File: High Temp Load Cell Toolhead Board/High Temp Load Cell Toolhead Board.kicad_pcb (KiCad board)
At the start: 4 copper layers, 60 x 60 mm, 118 parts, among them J1 Conn_01x03, J11 Conn_01x03, J12 Conn_01x03, J13 PinHeader_2x4_P2.54mm, J2 Conn_02x08, J6 Conn_01x04, J7 Conn_01x02, J8 Conn_01x04, J9 Conn_01x02, P1 USB_C_Plug_USB2.0, Q1 DMG3404L, Q2 DMG3404L, SW1 SW_SPST, U1 MAX31865xTP, U2 STM32F103CBU6TR, U3 SN74LVC2G17DSFR, U4 SN74AHC1G32QDBVRQ1, U5 ADS1220, X1 ECS-2520MVLC-080-BP-TR

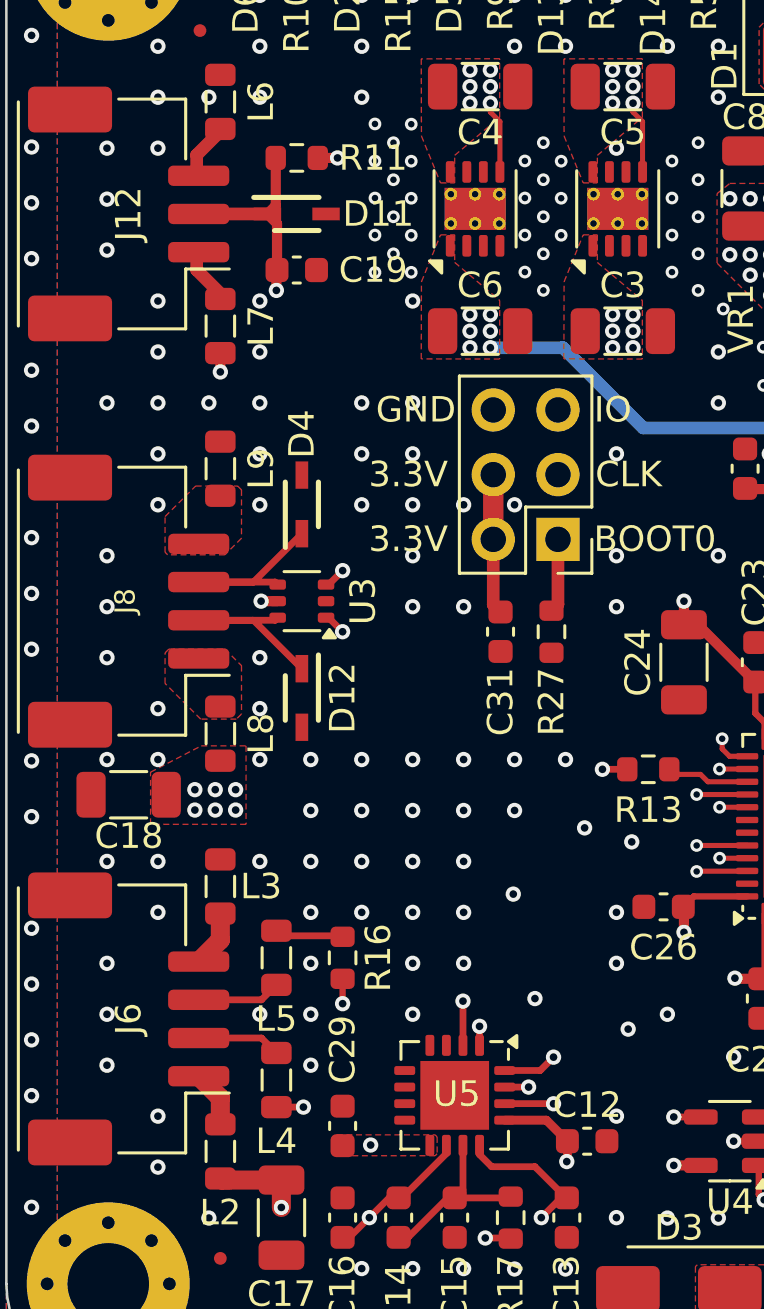
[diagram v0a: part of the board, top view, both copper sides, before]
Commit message: Add Net Class Directives
This change adds Net Class Directives for 3 types of specialized nets:
* ADC Signal - a net that may potentially be sensed by an ADC and should be treated as 50 Ohm impedance
* Digital Signal - a net that will have an oscillating digital signal on it but does not carry any power. This should also be treated as 50 Ohm impedance.
* Digital Pair - a differential digital pair. This is only used for the USB data pair which is 90 Ohm impedance.
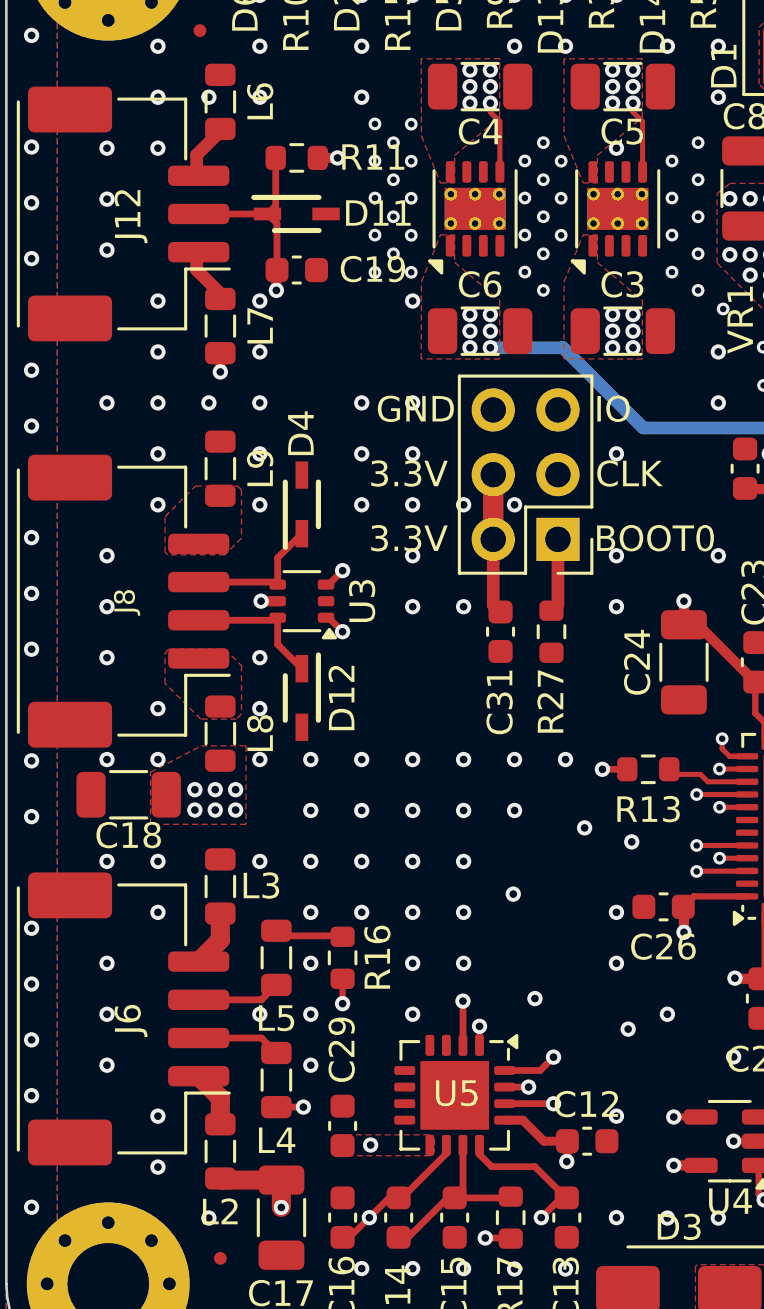
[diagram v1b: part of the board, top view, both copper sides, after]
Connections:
- net /INPUT_24V+ renamed /+24V_INPUT
- net /INPUT_FANV+ renamed /+FANV_INPUT
- net /SW_HEATSINK_4 renamed /SW_HEATSINK
- net SPI_2_SCLK renamed LED_MCU_CLK
- net SPI_2_SDO renamed LED_MCU_SDO
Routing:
- net /LED_SDI: track 7.98 -> 5.53 mm
- net /LED_CLK: track 7.98 -> 5.53 mm

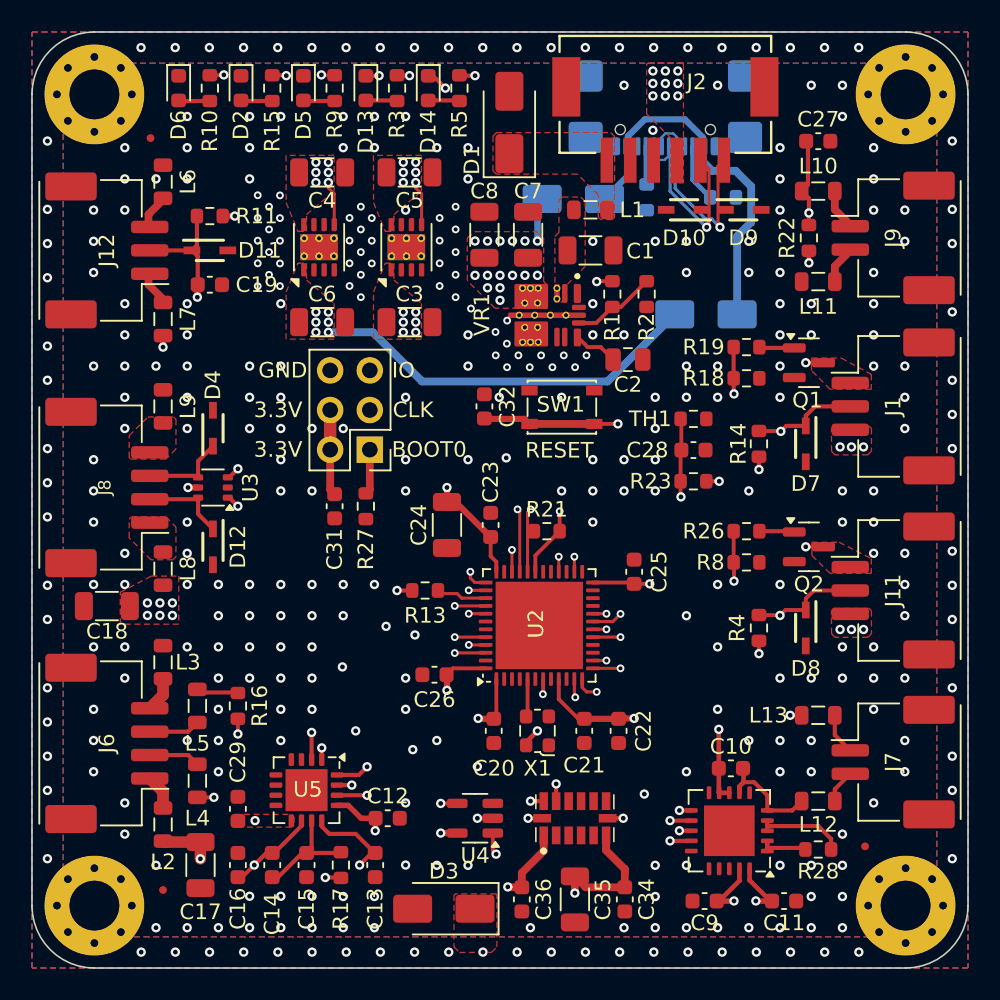
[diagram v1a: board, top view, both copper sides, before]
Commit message: More Targeted GND Paths
* Fix the TLVM23615RDNR footprint so its pads are plated
* Add GND vias in locations where via walls exist on layer 1
* Add GND vias or where a signal transitions across the core material between layer 2 and 3
* Add some GND vias near power decoupling capacitors
* Move the ADS1220 ADC signal lines down to layer 32 so they have 100% ground coverage across their length. They were passing under 5V caps and resistors.
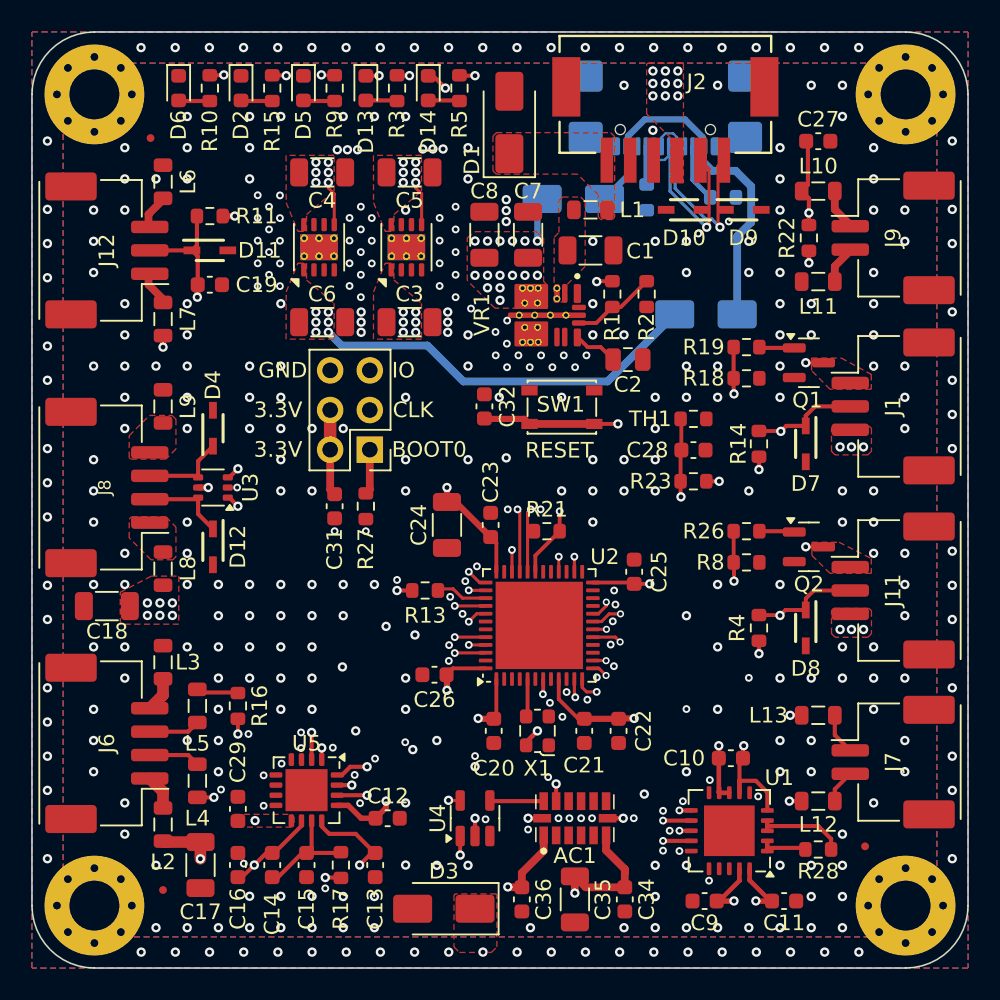
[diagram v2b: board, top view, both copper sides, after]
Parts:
- moved C10 0.65 mm to (44.8, 46.5)
- turned U4 to 90 degrees
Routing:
- net Net-(U1-FORCE+): track 7.77 -> 12.7 mm, vias 0 -> 2
- net Net-(AC1-SDA/SDI/SDIO): track 7.73 -> 3.47 mm, vias 2 -> 0
- net /FAN0_MOSFET_GND: track 46.3 -> 49.3 mm
- net /FAN1_MOSFET_GND: track 56.1 -> 59.0 mm
- net ADXL345_CS: track 21.8 -> 23.9 mm
- net SPI_1_SCLK: track 44.3 -> 43.1 mm
- net MAX31865_CS: track 17.7 -> 16.5 mm
- net USB_PULL_UP: track 47.4 -> 46.7 mm
- net Net-(U1-FORCE-): track 10.4 -> 9.79 mm
- net GND: vias 273 -> 340

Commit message: USB Routing Improvement & Trach Width Change
* Fix net class assignment of USB lines so they autoroute with the correct rules.
* Moved the LED CLK line routing so it doesn't cross the USB lines
* Added a zone of ground fill on layer 3 to cover the USB traces on the back of the board
* Changes the standard track with to 15mil / 0.381mm. This is what OSH Park say is 50 Ohm in their process.

Fixup

Fixup
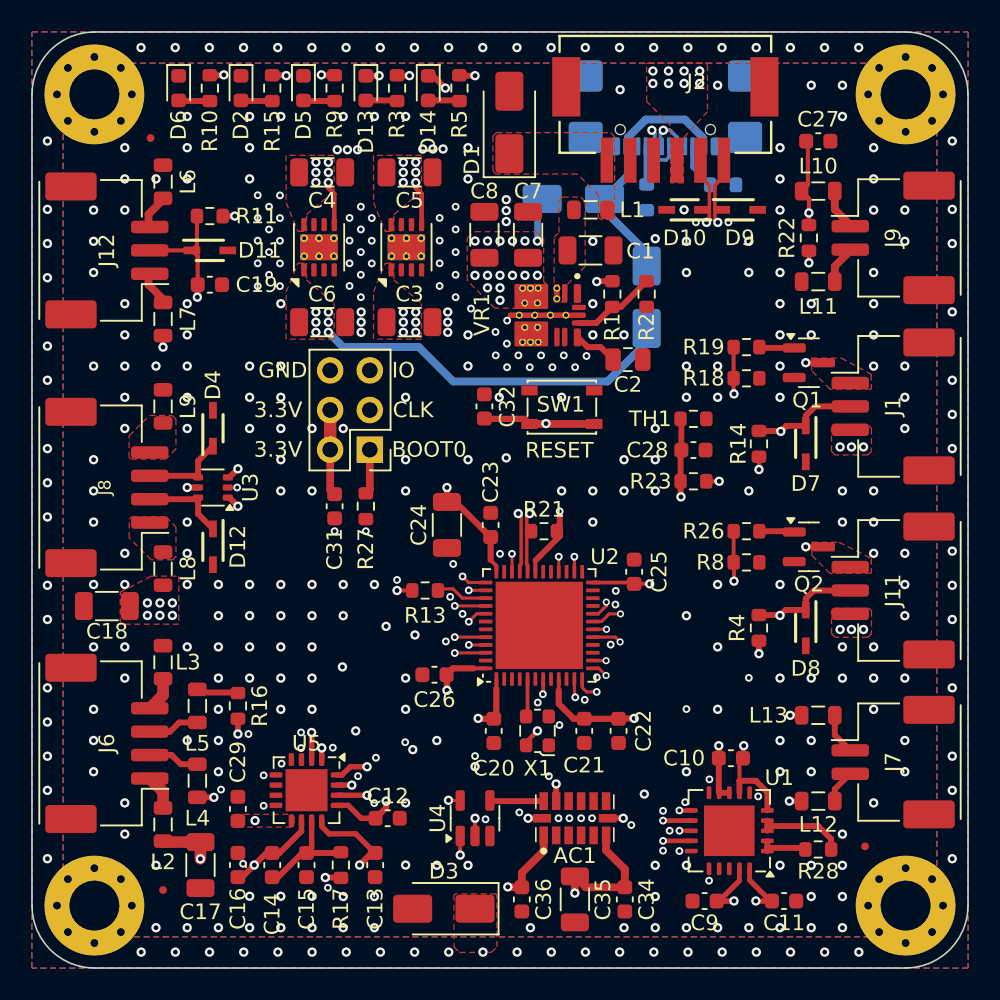
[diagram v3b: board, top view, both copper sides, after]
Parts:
- moved D16 3.96 mm to (39.4, 17.0), turned to 90 degrees
- moved R7 0.80 mm to (44.3, 9.80)
- moved D9 0.24 mm to (45.4, 11.4)
- moved R21 0.18 mm to (32.8, 32.0)
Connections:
- U2 pad 26: LED_MCU_CLK -> LED_MCU_SDO
- U2 pad 28: LED_MCU_SDO -> LED_MCU_CLK
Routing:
- net Net-(D15-A): track 24.2 -> 16.3 mm
- net LED_MCU_SDO: track 23.8 -> 28.5 mm
- net USB_D-: track 40.5 -> 44.6 mm, vias 2 -> 3
- net USB_D+: track 40.9 -> 43.8 mm, vias 2 -> 3
- net +5V: track 53.0 -> 51.3 mm
- net NRST: track 30.0 -> 31.1 mm
- net /FAN0_MOSFET_GND: track 49.3 -> 48.2 mm
- net LED_MCU_CLK: track 26.3 -> 27.1 mm
- net Net-(P1-CC2): track 3.74 -> 2.94 mm
- net FILAMENT_SW: track 41.8 -> 42.3 mm
- net /+FANV_INPUT: vias 17 -> 16
- net GND: vias 340 -> 331
